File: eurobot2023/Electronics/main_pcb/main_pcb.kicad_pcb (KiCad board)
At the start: 2 copper layers, 88 x 94 mm, 56 parts, among them IC1 CD74HCT125M96, IC2 SN74LVC126ADR, J1 PI40HAT, J10 Conn_01x02_Male, J11 MagneticEncoder, J13 MagneticEncoder, J14 Conn_01x03_Male, J15 Conn_01x02_Male, J16 Conn_02x02_Odd_Even, J17 Conn_02x02_Odd_Even, J18 Conn_02x02_Odd_Even, J2 Conn_01x02_Male, J20 Conn_01x03_Male, J21 Conn_01x03_Male, J24 Conn_01x03_Male, J3 Conn_01x02_Male, J4 Conn_01x02_Male, J5 Conn_01x02_Male, J6 Conn_01x02_Male, J7 Conn_01x02_Male, J8 Conn_01x02_Male, J9 22-03-5035, P1 R-78Bxx-2.0, P2 Amazon 10A stepdown, Q1 2SK4017_Q_, Q2 2SK4017_Q_, Q3 2SK4017_Q_, Q4 2SK4017_Q_, Q5 2SK4017_Q_, Q6 2SK4017_Q_, U1 MCP2515-xSO, U2 TJA1049T, U3 PCA9306D, U4 Pololu_MAX14870, U5 PCA9685PW, U6 Pololu_MAX14870

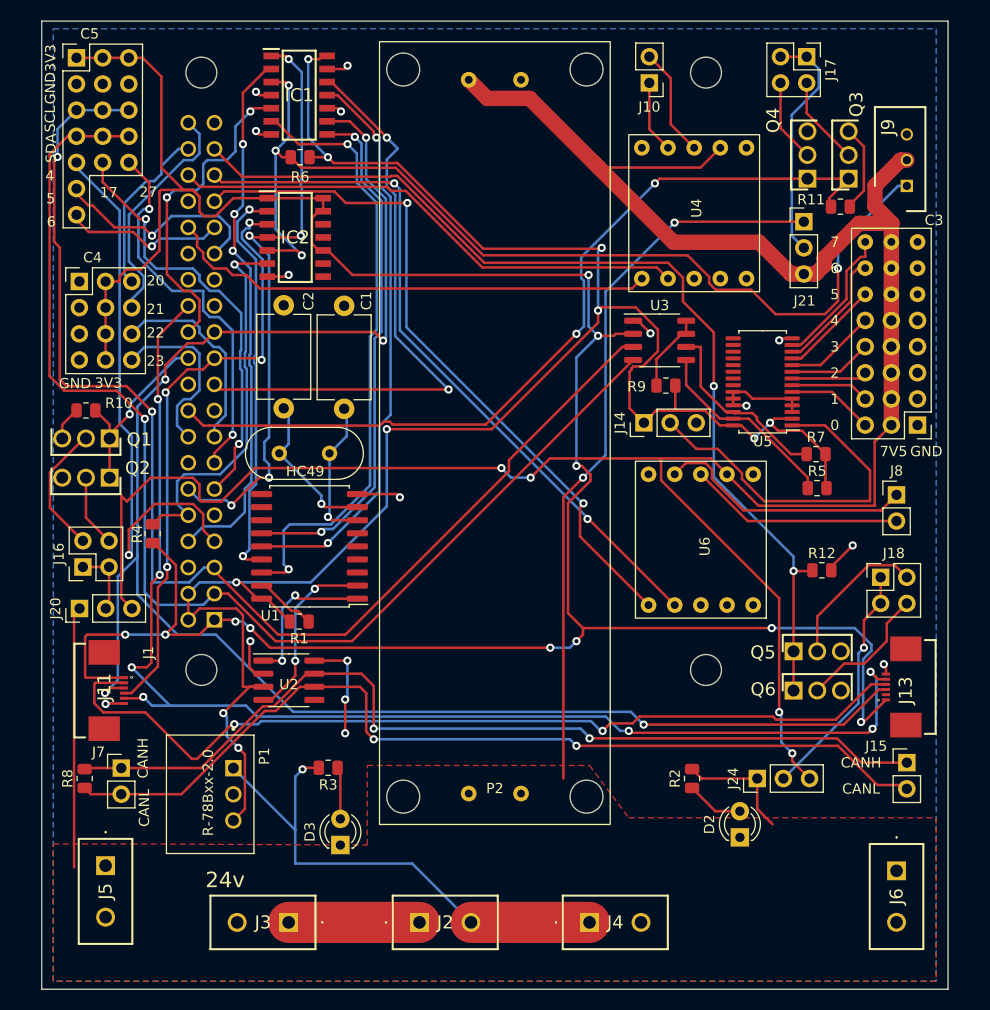
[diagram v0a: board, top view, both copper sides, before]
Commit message: Reroute 5v main pcb
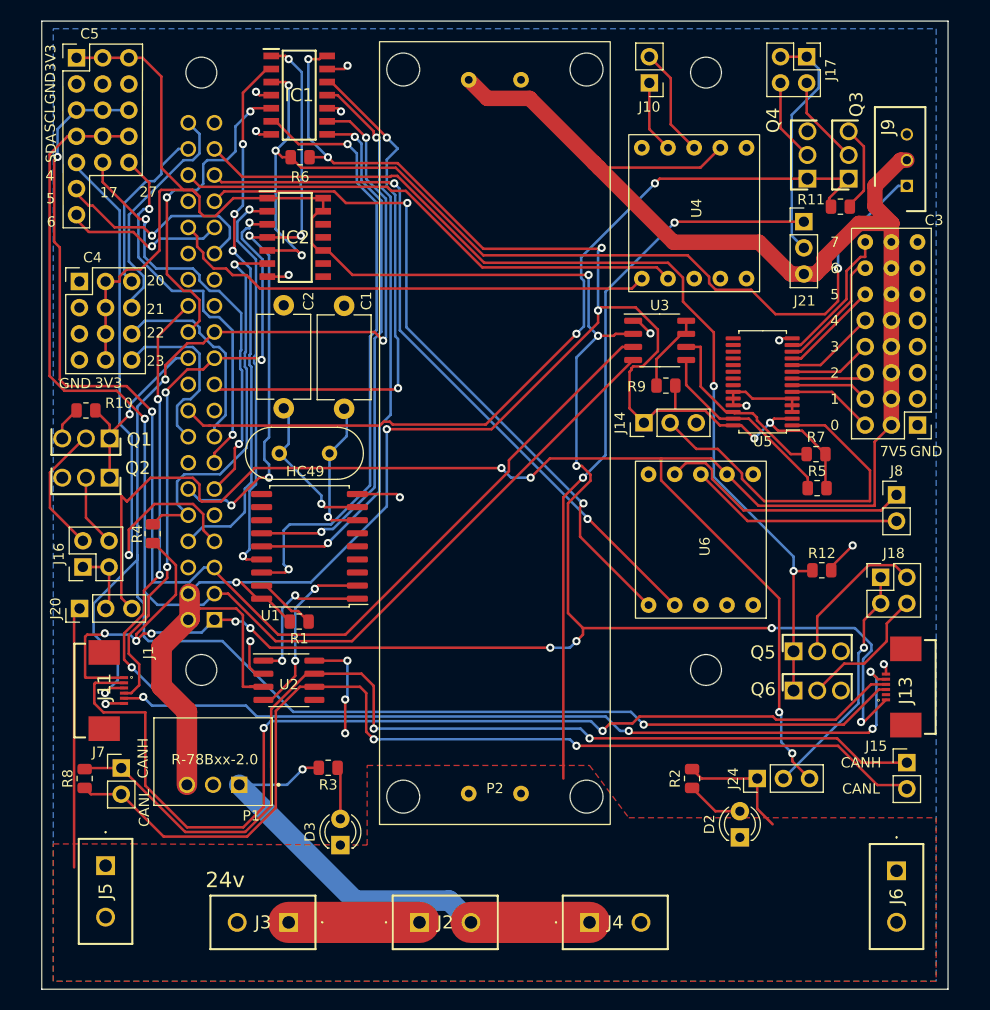
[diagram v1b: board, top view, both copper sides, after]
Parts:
- moved P1 1.71 mm to (89.2, 130.1), turned to 180 degrees
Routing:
- net Net-(J11-Pad2): track 87.9 -> 102.1 mm
- net Net-(J15-Pad1): track 89.7 -> 100.9 mm
- net Net-(J15-Pad2): track 90.7 -> 99.6 mm
- net /SPI1 MOSI: track 58.8 -> 51.8 mm
- net +5V: track 195.2 -> 200.5 mm, vias 10 -> 8
- net /SPI1 CLK: track 167.4 -> 171.3 mm
- net Net-(J2-Pad2): track 50.5 -> 48.0 mm
- net +3.3V: track 245.3 -> 247.7 mm, vias 11 -> 12
- net /SPI1 MISO: track 58.7 -> 59.6 mm

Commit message: Minor PCB fixups.
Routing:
- net Net-(J11-Pad2): track 102.1 -> 79.7 mm
- net Net-(J15-Pad1): track 100.9 -> 88.8 mm, vias 2 -> 3
- net +3.3V: track 247.7 -> 237.2 mm
- net Net-(J15-Pad2): track 99.6 -> 90.3 mm, vias 2 -> 3
- net GND: track 59.2 -> 50.6 mm, vias 16 -> 14
- net +5V: track 200.5 -> 196.4 mm
- net /SPI1_CS1: track 125.5 -> 123.5 mm, vias 7 -> 6
- net /SPI1 CLK: track 171.3 -> 169.5 mm
- net Net-(J2-Pad2): track 48.0 -> 49.7 mm
- net /SPI1 MISO: track 59.6 -> 60.5 mm
- net Net-(U1-Pad2): track 17.6 -> 16.8 mm
- net +24V: track 108.2 -> 107.4 mm
- net /GPIO 21: track 23.2 -> 22.6 mm

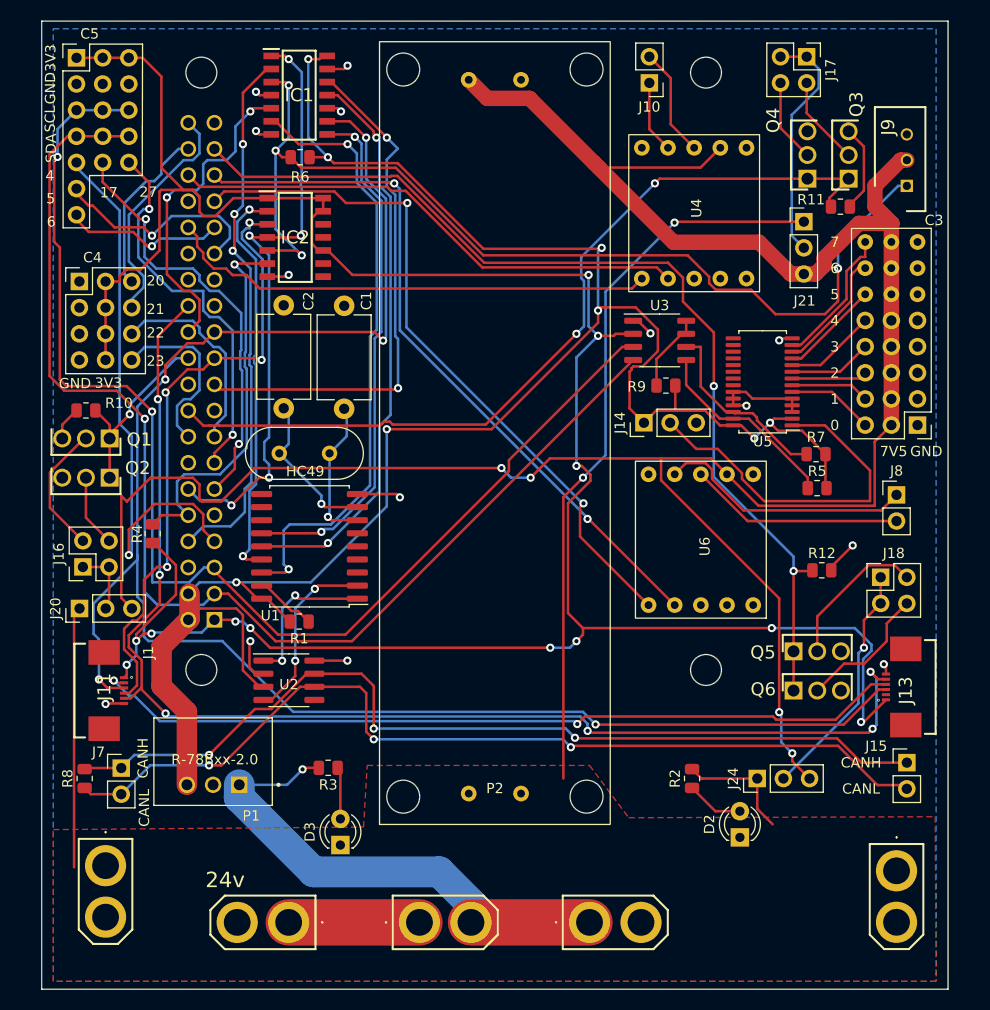
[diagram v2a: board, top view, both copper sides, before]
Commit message: Rework logger mechanism to make it more powerfull  - allow logging of arbitrary variables declared on the fly  - rely on HDF5 for long-term support  - use Teleplot for live debug
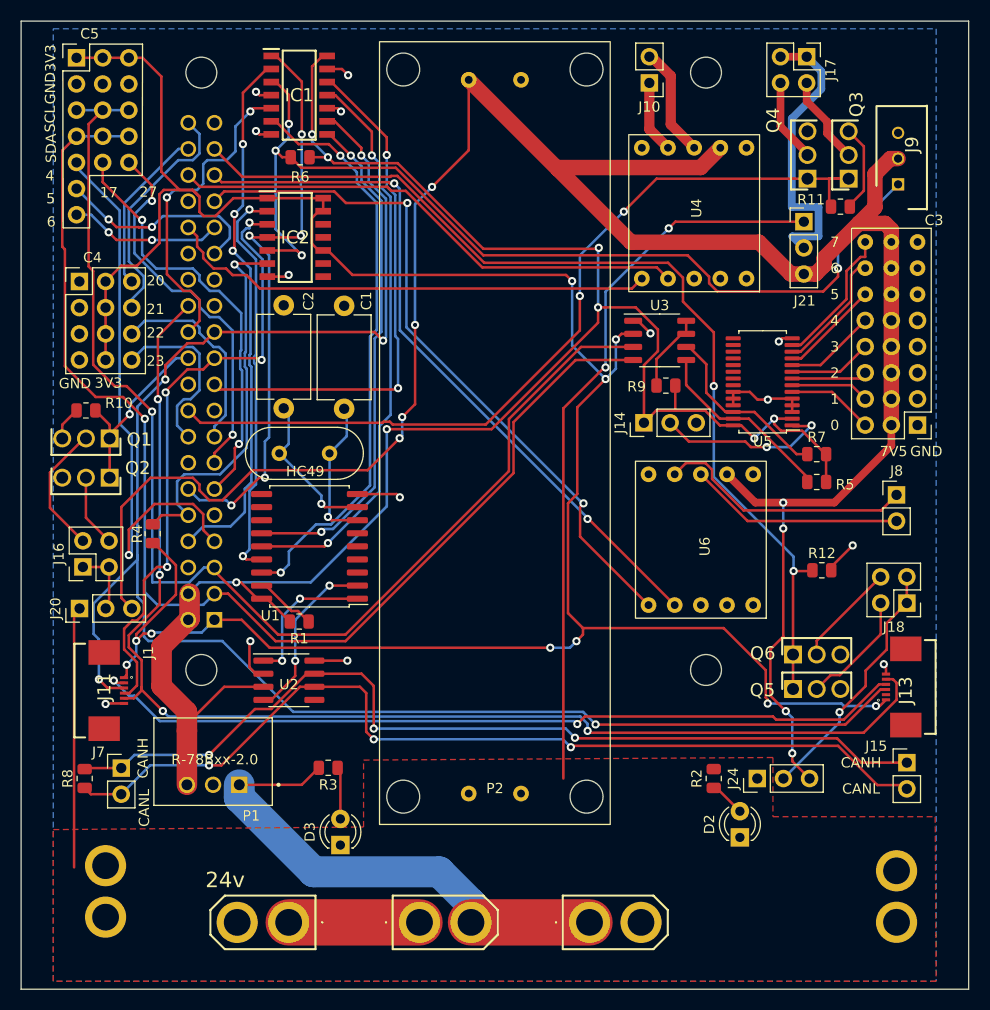
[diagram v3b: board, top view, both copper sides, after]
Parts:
- J5, J6: moved to B.Cu
- moved Q5 3.66 mm to (142.9, 120.8)
- moved J18 3.56 mm to (154.0, 112.5), turned to 180 degrees
- moved Q6 3.50 mm to (142.9, 117.5)
- moved R2 2.10 mm to (135.2, 129.5)
- moved J9 0.86 mm to (153.2, 71.8)
- moved R5 0.60 mm to (145.2, 100.8)
- moved R7 0.07 mm to (145.2, 98.0)
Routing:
- net /A0: track 35.2 -> 17.4 mm, vias 0 -> 2
- net +24V: track 107.4 -> 95.7 mm
- net +5V: track 196.4 -> 188.7 mm
- net Net-(J21-Pad2): track 23.2 -> 28.5 mm
- net +3.3V: track 237.2 -> 232.1 mm, vias 12 -> 10
- net /UART_HalfDuplex: track 100.0 -> 95.1 mm
- net +7.5V: track 229.5 -> 225.5 mm, vias 4 -> 8
- net /SPI1_CS0_5: track 59.4 -> 56.2 mm
- net Net-(J18-Pad2): track 14.6 -> 11.4 mm
- net Net-(J18-Pad4): track 13.2 -> 10.1 mm
- net Net-(D2-Pad2): track 5.58 -> 3.20 mm
- net /I2C SCL: track 121.2 -> 119.1 mm, vias 2 -> 1
- net /Servo DIR: track 59.0 -> 57.4 mm
- net /SPI1 CLK_5: track 51.0 -> 49.4 mm
- net /SPI1_CS1: track 123.5 -> 122.2 mm, vias 6 -> 4
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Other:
- board size 88 x 94 mm -> 92 x 94 mm
